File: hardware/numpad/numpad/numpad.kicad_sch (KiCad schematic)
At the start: 5 parts, among them J1 Conn_01x04, J2 Conn_01x04, J3 Conn_01x04, J4 Conn_01x04, U1 STM32F446RET6

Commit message: connectors for other modules
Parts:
- renumbered J4 to East, J1 to North, J3 to South, J2 to West
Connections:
- net P,+5: now reaches South.1 (Pin_1)
- net P,+5: now also East.4 (Pin_4), North.4 (Pin_4), West.1 (Pin_1)
- net P,E: now reaches South.4 (Pin_4)
- net P,E: now also East.1 (Pin_1), North.1 (Pin_1), West.4 (Pin_4)
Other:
- moved on the sheet: East, North, South, U1

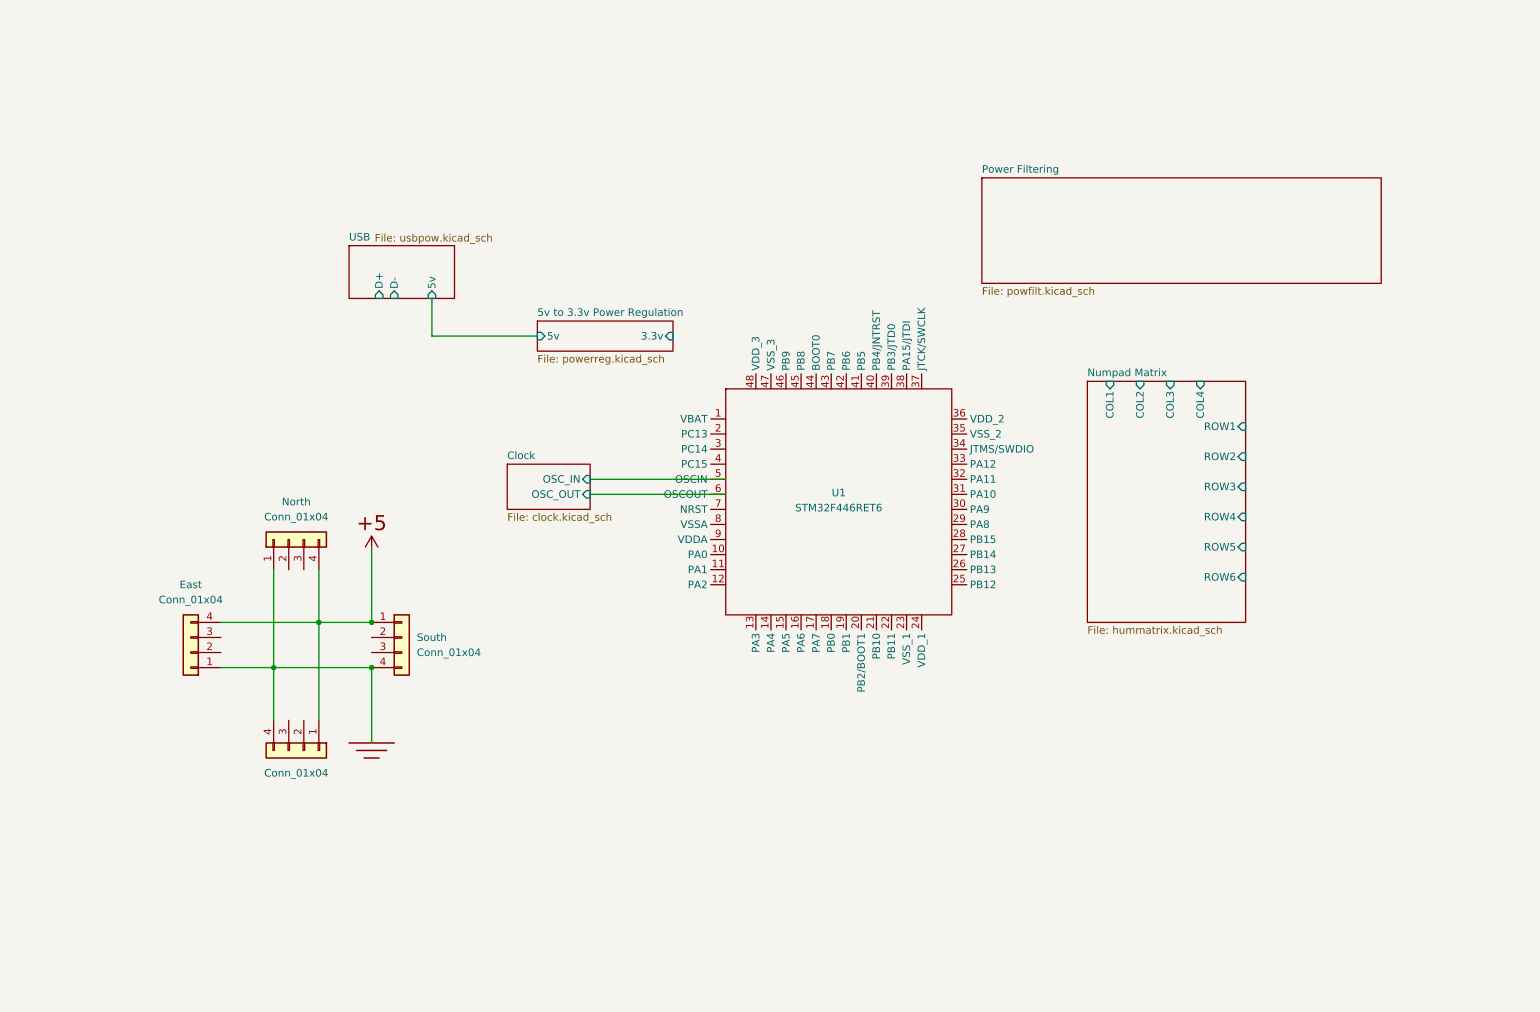
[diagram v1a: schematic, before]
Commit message: USB; Coupling Caps; and XTAL schematic
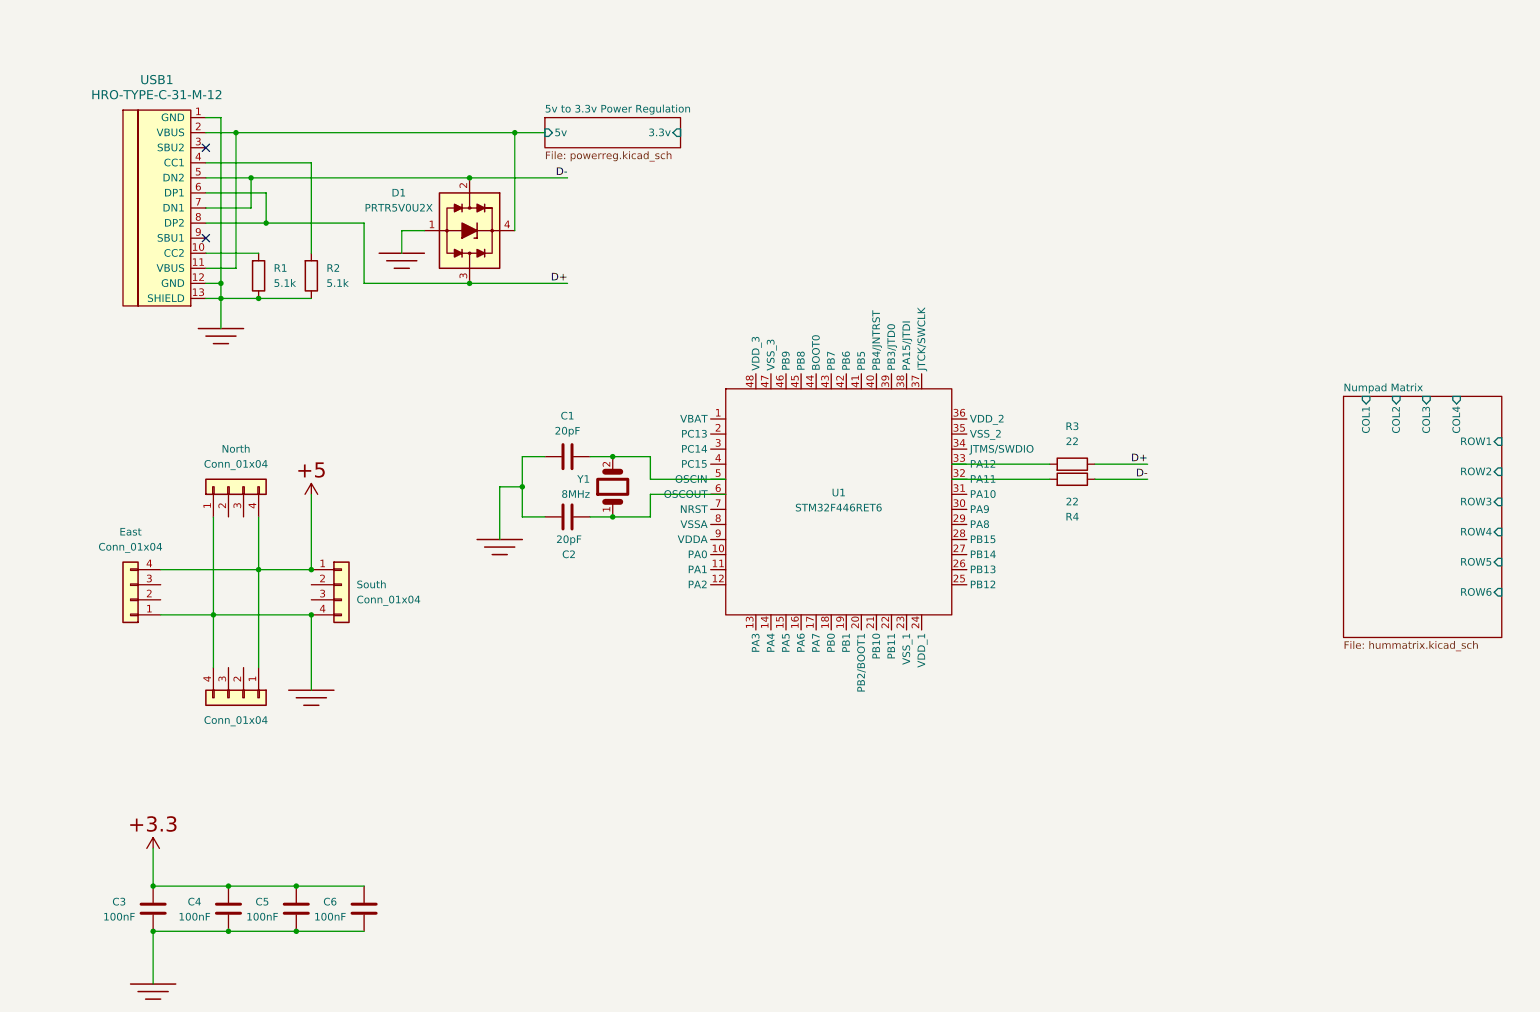
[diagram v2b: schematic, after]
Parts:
- added C1, C2: 20pF, PCM_Capacitor_SMD_AKL:C_0805_2012Metric, symbol PCM_Capacitor_AKL:C_0805
- added C3, C4, C5, C6: 100nF, PCM_Capacitor_SMD_AKL:C_0805_2012Metric, symbol PCM_Capacitor_AKL:C_0805
- added D1: PRTR5V0U2X, PCM_Package_TO_SOT_SMD_AKL:SOT-143, symbol PCM_Diode_TVS_AKL:PRTR5V0U2X
- added R1, R2: 5.1k, PCM_Resistor_SMD_AKL:R_0805_2012Metric, symbol PCM_Resistor_AKL:R_0805
- added R3, R4: 22, PCM_Resistor_SMD_AKL:R_0805_2012Metric, symbol PCM_Resistor_AKL:R_0805
- added USB1: HRO-TYPE-C-31-M-12, symbol Type-C:HRO-TYPE-C-31-M-12
- added Y1: 8MHz, PCM_Crystal_AKL:Crystal_HC52-U_Vertical, symbol PCM_SL_Devices:Crystal_8MHz
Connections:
- net 5v to 3.3v Power Regulation/5v: now also D1.4 (VP), USB1.11 (VBUS), USB1.2 (VBUS)
- net P,E: now also C1.2, C2.2, C3.2, C4.2, C5.2, C6.2, D1.1 (VN), R1.2, R2.2, USB1.1 (GND), USB1.12 (GND), USB1.13 (SHIELD)
- net at U1.32 (PA11): now also R4.1
- net at U1.33 (PA12): now also R3.1
- net Clock/OSC_IN: no longer names the net of U1.5 (OSCIN)
- net Clock/OSC_IN: now also C1.1, Y1.2
- net Clock/OSC_OUT: no longer names the net of U1.6 (OSCOUT)
- net Clock/OSC_OUT: now also C2.1, Y1.1
- new net: R1.1, USB1.10 (CC2)
- new net: R2.1, USB1.4 (CC1)
- new net D+: D1.3 (L2), R3.2, USB1.6 (DP1), USB1.8 (DP2)
- new net D-: D1.2 (L1), R4.2, USB1.5 (DN2), USB1.7 (DN1)
- new net P,+3.3: C3.1, C4.1, C5.1, C6.1
- no-connect marks 0 -> 2
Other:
- removed sheet Clock
- removed sheet Power Filtering
- removed sheet USB
- moved on the sheet: East, North, South

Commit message: numpad, connections, and more
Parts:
- removed West: Conn_01x04, 4ms_Connector:Pins_1x04_2.54mm_TH_SWD, symbol PCM_4ms_Connector:Conn_01x04
- added C10, C7: 1uF, PCM_Capacitor_SMD_AKL:C_0805_2012Metric, symbol PCM_Capacitor_AKL:C_0805
- added C8: 10uF, PCM_Capacitor_SMD_AKL:C_0805_2012Metric, symbol PCM_Capacitor_AKL:C_0805
- added C9: 4.7uF, PCM_Capacitor_SMD_AKL:C_0805_2012Metric, symbol PCM_Capacitor_AKL:C_0805
- added D2: D_Generic, symbol PCM_4ms_Diode:D_Generic
- added FB1: Ferrite_Bead, PCM_Fuse_AKL:Fuse_0805_2012Metric_Pad1.15x1.40mm_BigPads, symbol PCM_Device_AKL:Ferrite_Bead
- added IC1: LD1117-3.3V-SOT223, 4ms_Package_SOT:SOT223, symbol PCM_4ms_Regulator:LD1117-3.3V-SOT223
- added R5: 10k, PCM_Resistor_SMD_AKL:R_0805_2012Metric, symbol PCM_Resistor_AKL:R_0805
- added South: Conn_01x04, 4ms_Connector:Pins_1x04_2.54mm_TH_SWD, symbol PCM_4ms_Connector:Conn_01x04
- U1: value STM32F446RET6 -> ~; footprint footprints:LQFP64-10x10mm -> (none)
- renumbered South to East, East to West
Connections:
- net P,+3.3 is gone; now on net +3.3V: C3.1, C4.1, C5.1, C6.1
- net D+: now also R4.1; no longer R3.2
- net D-: now also R3.2; no longer R4.2
- net P,E: no longer C1.2, C2.2, C3.2, C4.2, C5.2, C6.2, East.4 (Pin_4), North.1 (Pin_1), R1.2, R2.2, USB1.1 (GND), USB1.12 (GND), USB1.13 (SHIELD), West.1 (Pin_1)
- net UART_RX_EAST: now reaches East.2 (Pin_2)
- net UART_RX_EAST: now also U1.43 (PA10)
- net UART_TX_EAST: now reaches East.3 (Pin_3)
- net UART_TX_EAST: now also U1.42 (PA9)
- net UART_RX_NORTH: now reaches North.2 (Pin_2)
- net UART_RX_NORTH: now also U1.54 (PD2)
- net UART_TX_NORTH: now reaches North.3 (Pin_3)
- net UART_TX_NORTH: now also U1.53 (PC12)
- net +3.3V: now reaches U1.32 (VDD)
- net +3.3V: now also U1.1 (VBAT), U1.19 (VDD), U1.48 (VDD), U1.64 (VDD), C10.1, C8.2, FB1.2, IC1.2 (OUT); no longer R4.1
- net at U1.33 (PB12): no longer R3.1
- net GNDA: now reaches U1.12 (VSSA)
- net at U1.13 (VDDA): now also FB1.1
- net UART_TX_WEST: now reaches U1.14 (PA0)
- net UART_TX_WEST: now also West.3 (Pin_3)
- net UART_RX_WEST: now reaches U1.15 (PA1)
- net UART_RX_WEST: now also West.2 (Pin_2)
- net UART_TX_SOUTH: now reaches U1.16 (PA2)
- net UART_TX_SOUTH: now also South.3 (Pin_3)
- net UART_RX_SOUTH: now reaches U1.17 (PA3)
- net UART_RX_SOUTH: now also South.2 (Pin_2)
- net GND: now reaches U1.18 (VSS)
- net GND: now also C1.2, C2.2, C3.2, C4.2, C5.2, C6.2, East.4 (Pin_4), North.1 (Pin_1), R1.2, R2.2, U1.31 (VSS), U1.47 (VSS), U1.63 (VSS), USB1.1 (GND), USB1.12 (GND), USB1.13 (SHIELD), West.1 (Pin_1), C10.2, C7.2, C8.1, C9.1, IC1.1 (ADJ), R5.1, South.4 (Pin_4)
- net at U1.30 (VCAP): now also C9.2
- net at U1.44 (PA11): now also R3.1
- net at U1.45 (PA12): now also R4.2
- net 5v to 3.3v Power Regulation/5v: no longer names the net of USB1.11 (VBUS), USB1.2 (VBUS)
- net 5v to 3.3v Power Regulation/5v: now also D2.2 (A); no longer D1.4 (VP)
- net P,+5 renamed +5V
- net +5V: now also D1.4 (VP), C7.1, D2.1 (K), IC1.3 (IN), South.1 (Pin_1)
- new net: R5.2, U1.60 (BOOT)
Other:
- removed sheet 5v to 3.3v Power Regulation
- removed sheet Numpad Matrix
- added sheet Numpad Matrix + Rotary Encoder (matrixrot.kicad_sch)
- note added: "Backflow Protection. We also gotta ask Eric"
- note added: "Dont know which ferrite bead to use. We gotta ask eric"
- moved on the sheet: C1, C2, C3, C4, C5, C6, D1, East, North, R1, R2, R3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

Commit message: progreers
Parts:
- East1: renamed from East; footprint 4ms_Connector:Pins_1x04_2.54mm_TH_SWD -> Connector_PinSocket_2.54mm:PinSocket_1x04_P2.54mm_Vertical
- North1: renamed from North; footprint 4ms_Connector:Pins_1x04_2.54mm_TH_SWD -> Connector_PinSocket_2.54mm:PinSocket_1x04_P2.54mm_Vertical
- South1: renamed from South; footprint 4ms_Connector:Pins_1x04_2.54mm_TH_SWD -> Connector_PinSocket_2.54mm:PinSocket_1x04_P2.54mm_Vertical
- U1: footprint (none) -> footprints:LQFP64-10x10mm
- USB1: footprint (none) -> Type-C.pretty-master:HRO-TYPE-C-31-M-12-HandSoldering
- West1: renamed from West; footprint 4ms_Connector:Pins_1x04_2.54mm_TH_SWD -> Connector_PinSocket_2.54mm:PinSocket_1x04_P2.54mm_Vertical
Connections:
- net P,E is gone; now on net GND: D1.1 (VN)
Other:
- sheet Numpad Matrix + Rotary Encoder ports: added COL1, COL2, COL3, COL4, COL5, ROT+, ROT-, ROT_VCC, ROW1, ROW2, ROW3, ROW4, ROW5, ROW6; removed none
- moved on the sheet: C7, C8, IC1

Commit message: stuff
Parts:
- added C11: 0.1uF, PCM_Capacitor_SMD_AKL:C_0805_2012Metric, symbol PCM_Capacitor_AKL:C_0805
- added J1: Conn_01x06, 4ms_Connector:Pins_1x06_2.54mm_TH_SWD, symbol PCM_4ms_Connector:Conn_01x06
- added R6, R7, R8, R9: 22, PCM_Resistor_SMD_AKL:R_0805_2012Metric, symbol PCM_Resistor_AKL:R_0805
- added SW2: Push_Button, Button_Switch_THT:SW_PUSH_6mm, symbol PCM_SL_Devices:Push_Button
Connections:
- net +3.3V: now also J1.1 (Pin_1)
- net GND: now also C11.1, J1.3 (Pin_3), SW2.2
- net JTMS: now reaches U1.46 (PA13)
- net JTMS: now also R7.2
- net JTCLK: now reaches U1.49 (PA14)
- net JTCLK: now also R6.2
- net SWO: now reaches U1.55 (PB3)
- net SWO: now also R9.2
- net NRST: now reaches U1.7 (NRST)
- net NRST: now also C11.2, R8.1, SW2.1
- new net: J1.4 (Pin_4), R7.1
- new net: J1.5 (Pin_5), R8.2
- new net: J1.2 (Pin_2), R6.1
- new net: J1.6 (Pin_6), R9.1
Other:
- note added: "Gotta ask eric for this one too"
- moved on the sheet: C1, C10, C2, C3, C4, C5, C6, C7, C8, C9, FB1, IC1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
